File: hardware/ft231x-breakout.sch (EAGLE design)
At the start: 27 parts, among them Q1 2N7002PW, U1 FTS31XS-U

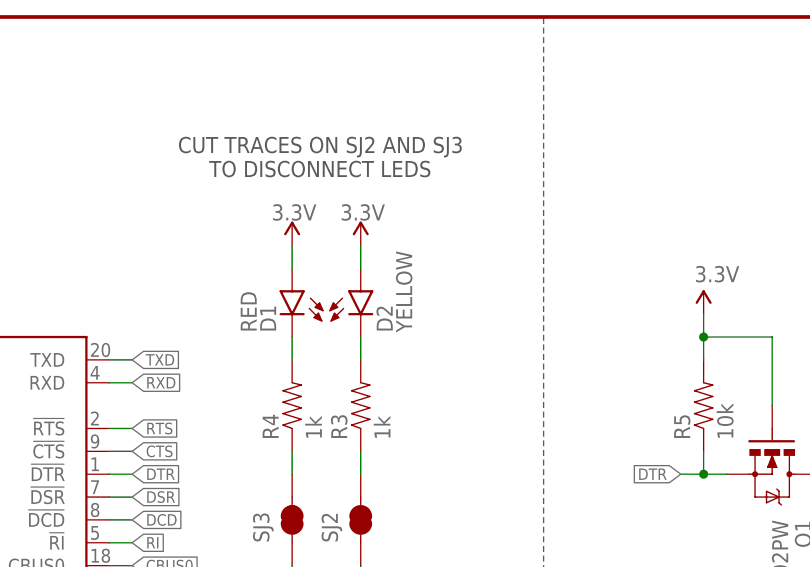
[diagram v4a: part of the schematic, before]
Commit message: Changed PCB dimension
Increased PCB dimension to better support USB connector.  Also slightly
adjusted the connector location itself to sit correctly on the PCB edge.
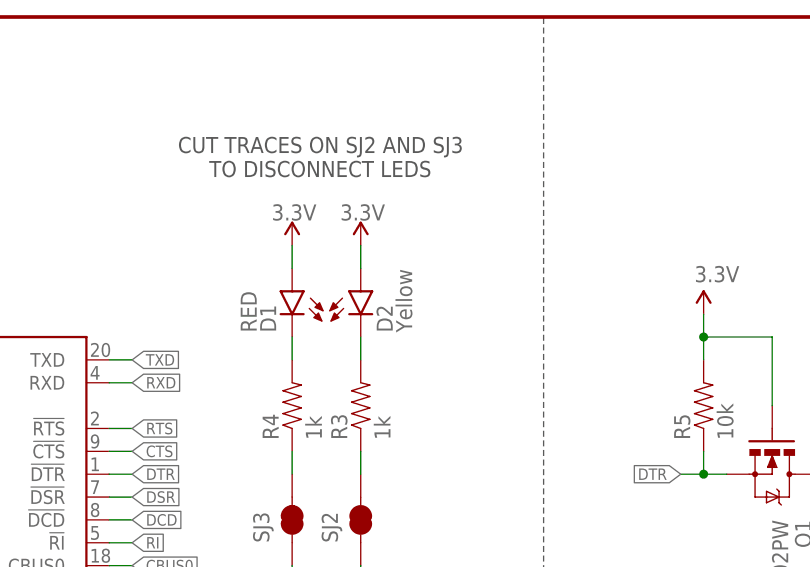
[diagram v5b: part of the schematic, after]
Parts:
- D2: value YELLOW -> Yellow
- JP2, JP4: device SparkFun-Connectors:M07NS -> SparkFun-Connectors:M07NO_SILK
- JP3: device SparkFun-Connectors:M06SIP-NS -> SparkFun-Connectors:M06NO_SILK_FEMALE_PTH
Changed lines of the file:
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@@
 <?xml version="1.0" encoding="utf-8"?>
 <!DOCTYPE eagle SYSTEM "eagle.dtd">
-<eagle version="7.1.0">
+<eagle version="7.4.0">
 <drawing>
 <settings>
@@
 <layer number="112" name="tSilk" color="7" fill="1" visible="yes" active="yes"/>
 <layer number="113" name="IDFDebug" color="4" fill="1" visible="yes" active="yes"/>
+<layer number="114" name="Badge_Outline" color="7" fill="1" visible="yes" active="yes"/>
+<layer number="115" name="ReferenceISLANDS" color="7" fill="1" visible="yes" active="yes"/>
 <layer number="116" name="Patch_BOT" color="9" fill="4" visible="no" active="yes"/>
 <layer number="118" name="Rect_Pads" color="7" fill="1" visible="yes" active="yes"/>
@@
 <part name="GND6" library="SparkFun-Aesthetics" deviceset="GND" device=""/>
 <part name="GND7" library="SparkFun-Aesthetics" deviceset="GND" device=""/>
-<part name="JP3" library="SparkFun-Connectors" deviceset="M06" device="SIP-NS"/>
+<part name="JP3" library="SparkFun-Connectors" deviceset="M06" device="NO_SILK_FEMALE_PTH"/>
 <part name="GND8" library="SparkFun-Aesthetics" deviceset="GND" device=""/>
 <part name="SJ1" library="SparkFun-Passives" deviceset="SOLDERJUMPER_2WAY" device="S"/>
@@
 <part name="C1" library="SparkFun-Capacitors" deviceset="10UF-16V-10%(TANT)" device="" value="10uF"/>
 <part name="D1" library="SparkFun-LED" deviceset="LED-RED" device="0603" value="RED"/>
-<part name="D2" library="SparkFun-LED" deviceset="LED-YELLOW" device="0603" value="YELLOW"/>
+<part name="D2" library="SparkFun-LED" deviceset="LED-YELLOW" device="0603" value="Yellow"/>
 <part name="R3" library="SparkFun-Resistors" deviceset="1MOHM1/10W1%(0603)" device="" value="1k"/>
 <part name="R4" library="SparkFun-Resistors" deviceset="1MOHM1/10W1%(0603)" device="" value="1k"/>
@@
 <part name="SJ2" library="SparkFun-Passives" deviceset="SOLDERJUMPER" device="TRACE" value="TXLED"/>
 <part name="SJ3" library="SparkFun-Passives" deviceset="JUMPER-PAD-2-NC_BY_TRACE" device="" value="RXLED"/>
-<part name="JP2" library="SparkFun-Connectors" deviceset="M07" device="NS"/>
-<part name="JP4" library="SparkFun-Connectors" deviceset="M07" device="NS"/>
+<part name="JP2" library="SparkFun-Connectors" deviceset="M07" device="NO_SILK"/>
+<part name="JP4" library="SparkFun-Connectors" deviceset="M07" device="NO_SILK"/>
 <part name="Q1" library="SparkFun-DiscreteSemi" deviceset="MOSFET-NCHANNEL" device="2N7002PW" value="2N7002PW"/>
 <part name="R5" library="SparkFun-Resistors" deviceset="10KOHM1/10W1%(0603)" device="0603" value="10k"/>

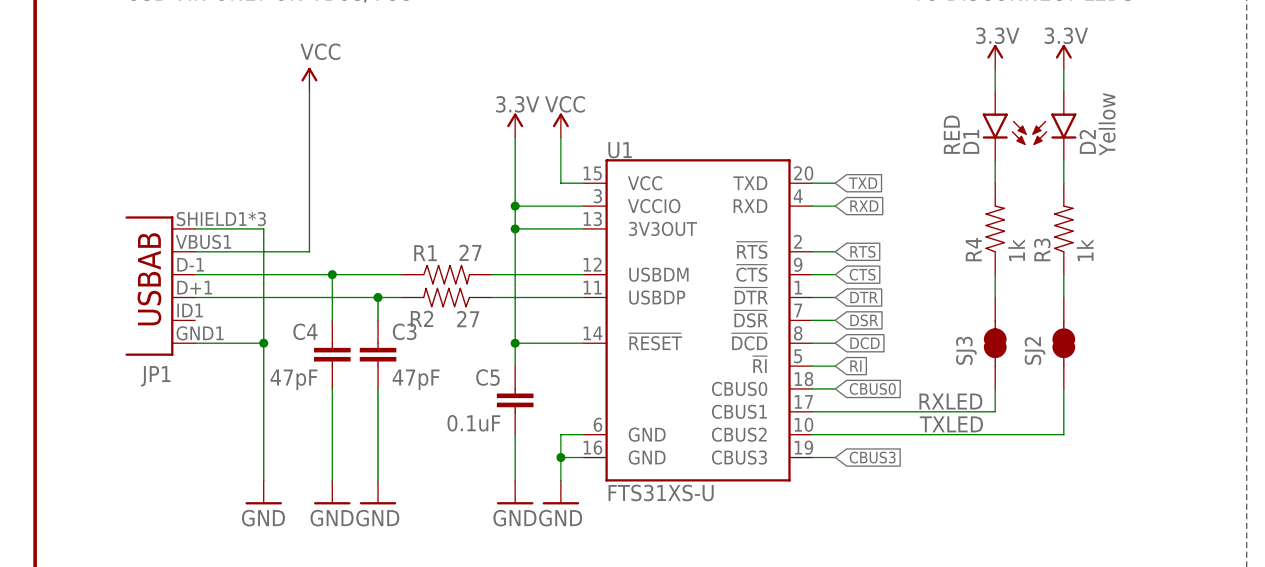
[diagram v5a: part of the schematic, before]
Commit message: Fixes to PROD_IDs on JP1, R3 and R4
Now they all have the correct PROD_ID for the part.
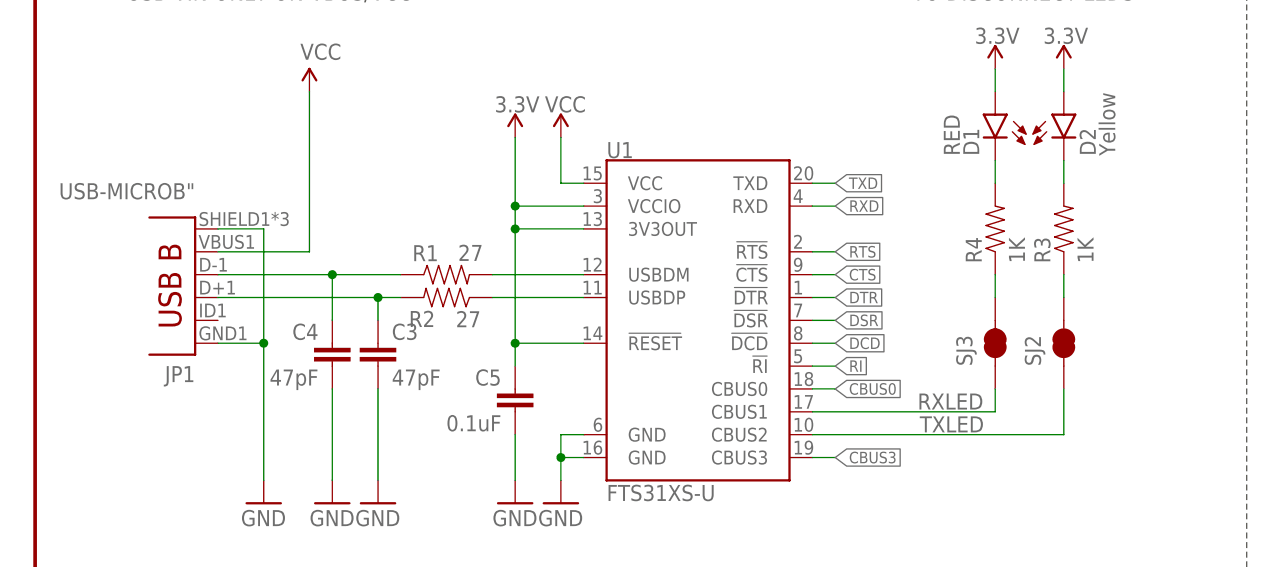
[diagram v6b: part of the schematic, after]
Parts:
- JP1: value (none) -> USB-MICROB"; device SparkFun-Connectors:USB-ABCONN-11794 -> SparkFun-Connectors:USB-MICROB"
- R3, R4: value 1k -> 1K; device SparkFun-Resistors:1MOHM1/10W1%(0603) -> SparkFun-Resistors:1KOHM-1/10W-1%(0603)
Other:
- moved on the sheet: JP1
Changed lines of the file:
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@@
 <part name="GND2" library="SparkFun-Aesthetics" deviceset="GND" device=""/>
 <part name="GND3" library="SparkFun-Aesthetics" deviceset="GND" device=""/>
-<part name="JP1" library="SparkFun-Connectors" deviceset="USB-AB" device="CONN-11794"/>
+<part name="JP1" library="SparkFun-Connectors" deviceset="USB-MICROB" device="&quot;"/>
 <part name="GND4" library="SparkFun-Aesthetics" deviceset="GND" device=""/>
 <part name="C5" library="SparkFun-Capacitors" deviceset="0.1UF-25V(+80/-20%)(0603)" device="" value="0.1uF"/>
@@
 <part name="D1" library="SparkFun-LED" deviceset="LED-RED" device="0603" value="RED"/>
 <part name="D2" library="SparkFun-LED" deviceset="LED-YELLOW" device="0603" value="Yellow"/>
-<part name="R3" library="SparkFun-Resistors" deviceset="1MOHM1/10W1%(0603)" device="" value="1k"/>
-<part name="R4" library="SparkFun-Resistors" deviceset="1MOHM1/10W1%(0603)" device="" value="1k"/>
+<part name="R3" library="SparkFun-Resistors" deviceset="1KOHM-1/10W-1%(0603)" device="" value="1K"/>
+<part name="R4" library="SparkFun-Resistors" deviceset="1KOHM-1/10W-1%(0603)" device="" value="1K"/>
 <part name="P+8" library="SparkFun-Aesthetics" deviceset="3.3V" device=""/>
 <part name="P+9" library="SparkFun-Aesthetics" deviceset="3.3V" device=""/>
@@
 <instance part="GND2" gate="1" x="38.1" y="111.76"/>
 <instance part="GND3" gate="1" x="58.42" y="111.76"/>
-<instance part="JP1" gate="G$1" x="12.7" y="134.62" rot="R180"/>
+<instance part="JP1" gate="G$1" x="15.24" y="137.16" rot="R180"/>
 <instance part="GND4" gate="1" x="25.4" y="111.76"/>
 <instance part="C5" gate="G$1" x="53.34" y="121.92" rot="MR0"/>
@@
 <wire x1="40.64" y1="134.62" x2="38.1" y2="134.62" width="0.1524" layer="91"/>
 <wire x1="38.1" y1="134.62" x2="38.1" y2="132.08" width="0.1524" layer="91"/>
-<wire x1="38.1" y1="134.62" x2="17.78" y2="134.62" width="0.1524" layer="91"/>
+<wire x1="38.1" y1="134.62" x2="20.32" y2="134.62" width="0.1524" layer="91"/>
 <junction x="38.1" y="134.62"/>
 <pinref part="JP1" gate="G$1" pin="D+"/>
@@
 <junction x="33.02" y="137.16"/>
 <pinref part="JP1" gate="G$1" pin="D-"/>
-<wire x1="33.02" y1="137.16" x2="17.78" y2="137.16" width="0.1524" layer="91"/>
+<wire x1="33.02" y1="137.16" x2="20.32" y2="137.16" width="0.1524" layer="91"/>
 </segment>
 </net>
@@
 <segment>
 <pinref part="JP1" gate="G$1" pin="GND"/>
-<wire x1="17.78" y1="129.54" x2="25.4" y2="129.54" width="0.1524" layer="91"/>
+<wire x1="20.32" y1="129.54" x2="25.4" y2="129.54" width="0.1524" layer="91"/>
 <wire x1="25.4" y1="129.54" x2="25.4" y2="114.3" width="0.1524" layer="91"/>
 <pinref part="GND4" gate="1" pin="GND"/>
 <pinref part="JP1" gate="G$1" pin="SHIELD"/>
-<wire x1="17.78" y1="142.24" x2="25.4" y2="142.24" width="0.1524" layer="91"/>
+<wire x1="20.32" y1="142.24" x2="25.4" y2="142.24" width="0.1524" layer="91"/>
 <wire x1="25.4" y1="142.24" x2="25.4" y2="129.54" width="0.1524" layer="91"/>
 <junction x="25.4" y="129.54"/>
@@
 <segment>
 <pinref part="JP1" gate="G$1" pin="VBUS"/>
-<wire x1="17.78" y1="139.7" x2="30.48" y2="139.7" width="0.1524" layer="91"/>
+<wire x1="20.32" y1="139.7" x2="30.48" y2="139.7" width="0.1524" layer="91"/>
 <pinref part="P+1" gate="G$1" pin="VCC"/>
 <wire x1="30.48" y1="139.7" x2="30.48" y2="157.48" width="0.1524" layer="91"/>
